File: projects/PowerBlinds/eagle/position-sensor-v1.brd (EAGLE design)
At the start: 66 x 40.6 mm, 22 parts, among them Q1 MAX481SO08, U1 ACS712ELCTR-20A-T

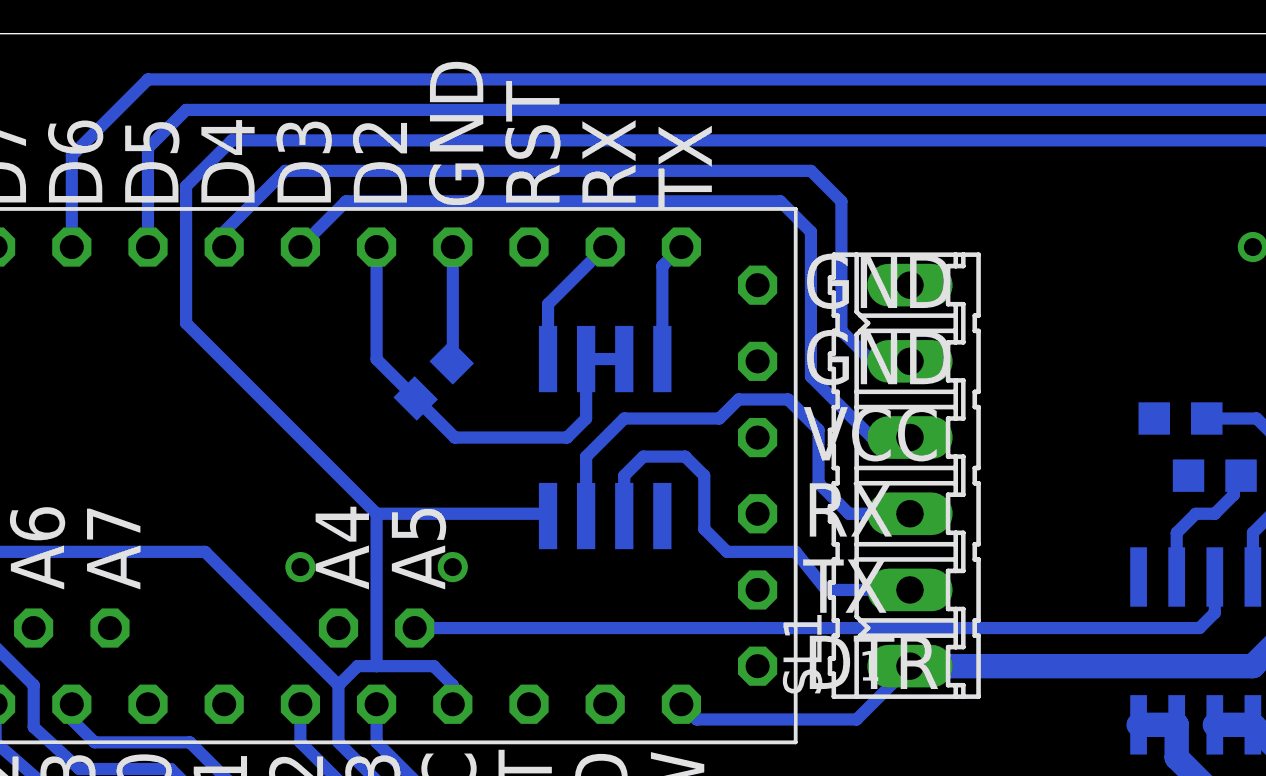
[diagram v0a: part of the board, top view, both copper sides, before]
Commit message: Power blinds: adding external pull-up resistors for inputs, and adding TVS diode for RS-485
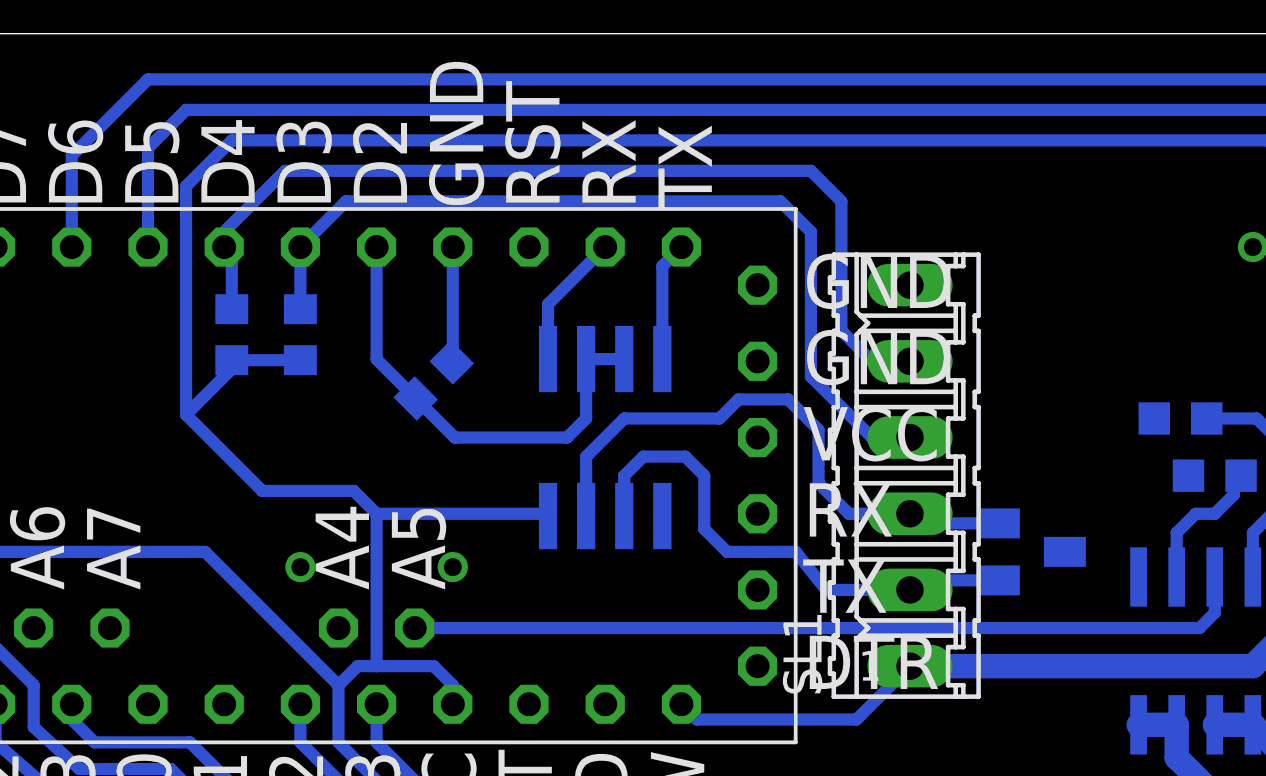
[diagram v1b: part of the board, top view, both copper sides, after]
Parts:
- added D1: SM712, serge:SOT23-3
- added R8, R9: 4.3M, adafruit:R0603
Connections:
- net +5V: now also R8.2, R9.2
- net D3: now also R8.1
- net D4: now also R9.1
- net GND: now also D1.3
- net N$1: now also D1.1
- net N$2: now also D1.2
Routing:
- net +5V: track 173.5 -> 180.1 mm
- net N$2: track 16.4 -> 19.5 mm
- net N$1: track 14.1 -> 17.2 mm
- net D4: track 29.4 -> 31.5 mm
- net D3: track 27.0 -> 29.1 mm
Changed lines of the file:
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@@
 <attribute name="OC_FARNELL" value="unknown" x="39.37" y="25.908" size="1.778" layer="27" rot="R90" display="off"/>
 </element>
+<element name="R8" library="adafruit" package="R0603" value="4.3M" x="19.05" y="30.607" rot="MR270"/>
+<element name="R9" library="adafruit" package="R0603" value="4.3M" x="16.764" y="30.607" rot="MR270"/>
+<element name="D1" library="serge" package="SOT23-3" value="SM712" x="43.434" y="23.368" rot="MR90"/>
 </elements>
 <signals>
@@
 <wire x1="44.45" y1="5.588" x2="44.45" y2="10.8712" width="0.4064" layer="16"/>
 <wire x1="44.45" y1="10.8712" x2="45.72" y2="12.1412" width="0.4064" layer="16"/>
+<contactref element="D1" pad="3"/>
+<wire x1="34.29" y1="32.258" x2="39.37" y2="32.258" width="0" layer="19" extent="1-1"/>
+<wire x1="31.115" y1="24.5618" x2="34.29" y2="29.718" width="0" layer="19" extent="16-16"/>
 <wire x1="19.05" y1="22.86" x2="24.13" y2="22.86" width="0" layer="19" extent="1-1"/>
-<wire x1="34.29" y1="29.718" x2="31.115" y2="24.5618" width="0" layer="19" extent="16-16"/>
-<wire x1="39.37" y1="32.258" x2="34.29" y2="32.258" width="0" layer="19" extent="1-1"/>
 <wire x1="24.09604375" y1="29.684040625" x2="24.13" y2="22.86" width="0" layer="19" extent="16-16"/>
 </signal>
@@
 <wire x1="8.89" y1="23.368" x2="15.875" y2="23.368" width="0.4064" layer="16"/>
 <wire x1="15.875" y1="23.368" x2="20.32" y2="18.923" width="0.4064" layer="16"/>
-<wire x1="15.24" y1="30.988" x2="21.59" y2="24.638" width="0.4064" layer="16"/>
 <wire x1="21.59" y1="24.638" x2="27.2288" y2="24.638" width="0.4064" layer="16"/>
 <wire x1="27.2288" y1="24.638" x2="27.305" y2="24.5618" width="0.4064" layer="16"/>
@@
 <wire x1="51.308" y1="37.084" x2="16.764" y2="37.084" width="0.4064" layer="16"/>
 <wire x1="16.764" y1="37.084" x2="15.24" y2="35.56" width="0.4064" layer="16"/>
-<wire x1="15.24" y1="35.56" x2="15.24" y2="30.988" width="0.4064" layer="16"/>
+<wire x1="15.24" y1="35.56" x2="15.24" y2="27.94" width="0.4064" layer="16"/>
 <wire x1="21.59" y1="24.638" x2="21.59" y2="19.558" width="0.4064" layer="16"/>
 <wire x1="23.241" y1="14.097" x2="20.32" y2="17.018" width="0.4064" layer="16"/>
@@
 <wire x1="10.16" y1="17.526" x2="10.16" y2="18.923" width="0.4064" layer="16"/>
 <wire x1="10.16" y1="18.923" x2="7.62" y2="21.463" width="0.4064" layer="16"/>
+<contactref element="R9" pad="2"/>
+<contactref element="R8" pad="2"/>
+<wire x1="15.24" y1="27.94" x2="17.78" y2="25.4" width="0.4064" layer="16"/>
+<wire x1="17.78" y1="25.4" x2="20.828" y2="25.4" width="0.4064" layer="16"/>
+<wire x1="20.828" y1="25.4" x2="21.59" y2="24.638" width="0.4064" layer="16"/>
+<wire x1="16.764" y1="29.757" x2="16.764" y2="29.464" width="0.4064" layer="16"/>
+<wire x1="16.764" y1="29.464" x2="15.24" y2="27.94" width="0.4064" layer="16"/>
+<wire x1="16.764" y1="29.757" x2="19.05" y2="29.757" width="0.4064" layer="16"/>
 <wire x1="27.305" y1="24.5618" x2="34.29" y2="27.178" width="0" layer="19" extent="16-16"/>
 </signal>
@@
 <wire x1="35.56" y1="23.368" x2="36.576" y2="22.098" width="0.4064" layer="16"/>
 <wire x1="36.576" y1="22.098" x2="39.37" y2="22.098" width="0.4064" layer="16"/>
+<contactref element="D1" pad="1"/>
+<wire x1="42.334" y1="22.418" x2="39.69" y2="22.418" width="0.4064" layer="16"/>
+<wire x1="39.69" y1="22.418" x2="39.37" y2="22.098" width="0.4064" layer="16"/>
 </signal>
 <signal name="N$2">
@@
 <wire x1="36.322" y1="25.654" x2="37.338" y2="24.638" width="0.4064" layer="16"/>
 <wire x1="37.338" y1="24.638" x2="39.37" y2="24.638" width="0.4064" layer="16"/>
+<contactref element="D1" pad="2"/>
+<wire x1="42.334" y1="24.318" x2="39.69" y2="24.318" width="0.4064" layer="16"/>
+<wire x1="39.69" y1="24.318" x2="39.37" y2="24.638" width="0.4064" layer="16"/>
 </signal>
 <signal name="V+">
@@
 <wire x1="37.084" y1="30.734" x2="38.1" y2="29.718" width="0.4064" layer="16"/>
 <wire x1="38.1" y1="29.718" x2="39.37" y2="29.718" width="0.4064" layer="16"/>
+<contactref element="R9" pad="1"/>
+<wire x1="16.764" y1="31.457" x2="16.764" y2="33.274" width="0.4064" layer="16"/>
+<wire x1="16.764" y1="33.274" x2="16.51" y2="33.528" width="0.4064" layer="16"/>
 </signal>
 <signal name="D3">
@@
 <wire x1="39.37" y1="27.178" x2="38.1" y2="27.178" width="0.4064" layer="16"/>
 <wire x1="38.1" y1="27.178" x2="36.068" y2="29.21" width="0.4064" layer="16"/>
+<contactref element="R8" pad="1"/>
+<wire x1="19.05" y1="31.457" x2="19.05" y2="33.528" width="0.4064" layer="16"/>
 </signal>
 <signal name="N$3">
